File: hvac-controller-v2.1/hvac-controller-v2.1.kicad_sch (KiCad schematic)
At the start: 45 parts, among them J1 Conn_M5Stamp_Pico_01x09_Female, J2 Conn_M5Stamp_Pico_01x04_Female, J3 Conn_01x06, J4 Conn_M5Stamp_Pico_01x06_Female, J5 VAC IN, U1 TPS5430DDA, U2 TPS5430DDA, U3 LM324DT

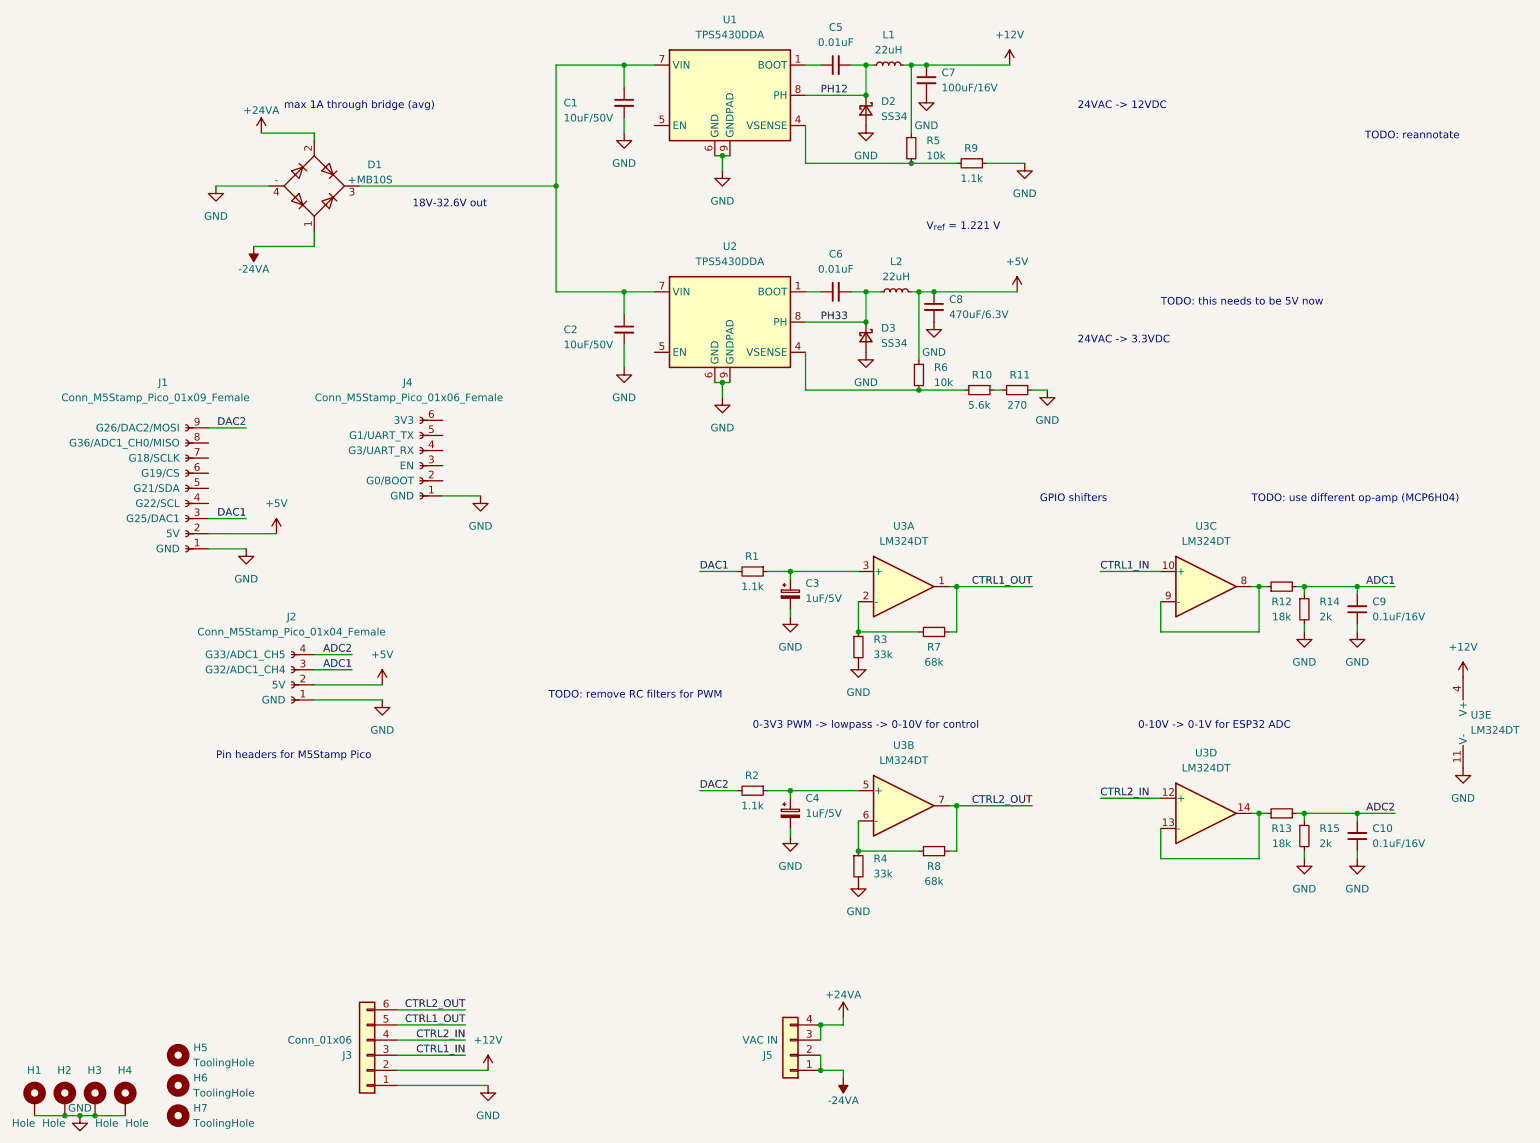
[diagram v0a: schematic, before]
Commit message: Add v2.1 and v3
To try to make it smaller
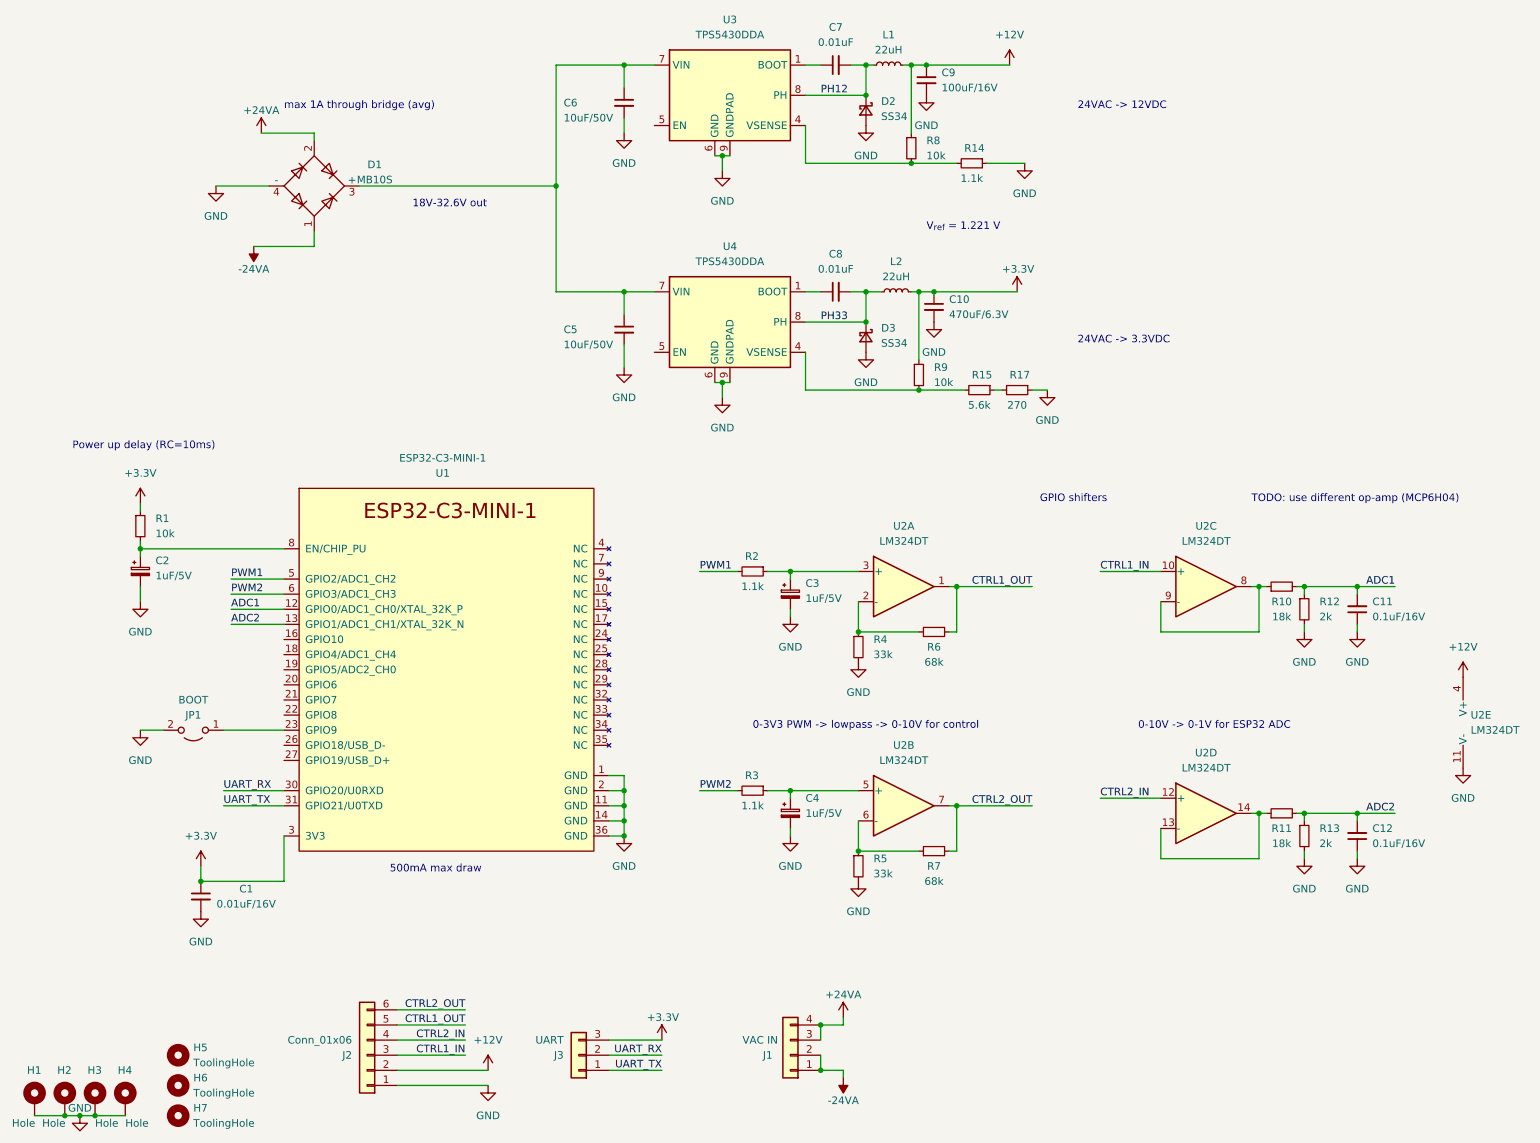
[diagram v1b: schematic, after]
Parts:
- removed J1: Conn_M5Stamp_Pico_01x09_Female, Connector_PinSocket_2.54mm:PinSocket_1x09_P2.54mm_Vertical, symbol kelvie:Conn_M5Stamp_Pico_1x9
- removed J2: Conn_M5Stamp_Pico_01x04_Female, Connector_PinSocket_2.54mm:PinSocket_1x04_P2.54mm_Vertical, symbol kelvie:Conn_M5Stamp_Pico_01x04_Female
- removed J4: Conn_M5Stamp_Pico_01x06_Female, Connector_PinSocket_2.54mm:PinSocket_1x06_P2.54mm_Vertical, symbol kelvie:Conn_M5Stamp_Pico_01x06_Female
- added C1: 0.01uF/16V, Capacitor_SMD:C_0402_1005Metric, symbol Device:C_Small
- added C2: 1uF/5V, Capacitor_SMD:C_0402_1005Metric, symbol Device:C_Polarized_Small
- added J3: UART, Connector_Wire:SolderWire-0.1sqmm_1x03_P3.6mm_D0.4mm_OD1mm, symbol Connector_Generic:Conn_01x03
- added JP1: BOOT, Jumper:SolderJumper-2_P1.3mm_Open_RoundedPad1.0x1.5mm, symbol Jumper:Jumper_2_Open
- added R1: 10k, Resistor_SMD:R_0402_1005Metric, symbol Device:R_Small
- added U1: ESP32-C3-MINI-1, Espressif:ESP32-C3-MINI-1, symbol Espressif:ESP32-C3-MINI-1
- renumbered C8 to C10, C9 to C11, C10 to C12, C2 to C5, C1 to C6, C5 to C7, C6 to C8, C7 to C9, J5 to J1, J3 to J2, R12 to R10, R13 to R11, R14 to R12, R15 to R13, R9 to R14, R10 to R15, R11 to R17, R1 to R2, R2 to R3, R3 to R4, R4 to R5, R7 to R6, R8 to R7, R5 to R8, R6 to R9, U3 to U2, U1 to U3, U2 to U4
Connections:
- net ADC1: now also U1.12 (GPIO0/ADC1_CH0/XTAL_32K_P)
- net ADC2: now also U1.13 (GPIO1/ADC1_CH1/XTAL_32K_N)
- net GND: now also C1.2, C2.2, JP1.2 (B), U1.1 (GND), U1.11 (GND), U1.14 (GND), U1.2 (GND), U1.36 (GND)
- net +5V renamed +3V3
- net +3V3: now also C1.1, J3.3 (Pin_3), R1.1, U1.3 (3V3)
- net DAC1 renamed PWM1
- net PWM1: now also U1.5 (GPIO2/ADC1_CH2)
- net DAC2 renamed PWM2
- net PWM2: now also U1.6 (GPIO3/ADC1_CH3)
- new net: C2.1, R1.2, U1.8 (EN/CHIP_PU)
- new net: JP1.1 (A), U1.23 (GPIO9)
- new net UART_RX: J3.2 (Pin_2), U1.30 (GPIO20/U0RXD)
- new net UART_TX: J3.1 (Pin_1), U1.31 (GPIO21/U0TXD)
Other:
- note added: "500mA max draw"
- note added: "Power up delay (RC=10ms)"
- note removed: "Pin headers for M5Stamp Pico"
- note removed: "TODO: reannotate"
- note removed: "TODO: remove RC filters for PWM"
- note removed: "TODO: this needs to be 5V now"
